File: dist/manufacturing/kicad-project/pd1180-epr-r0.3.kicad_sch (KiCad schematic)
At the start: 0 parts

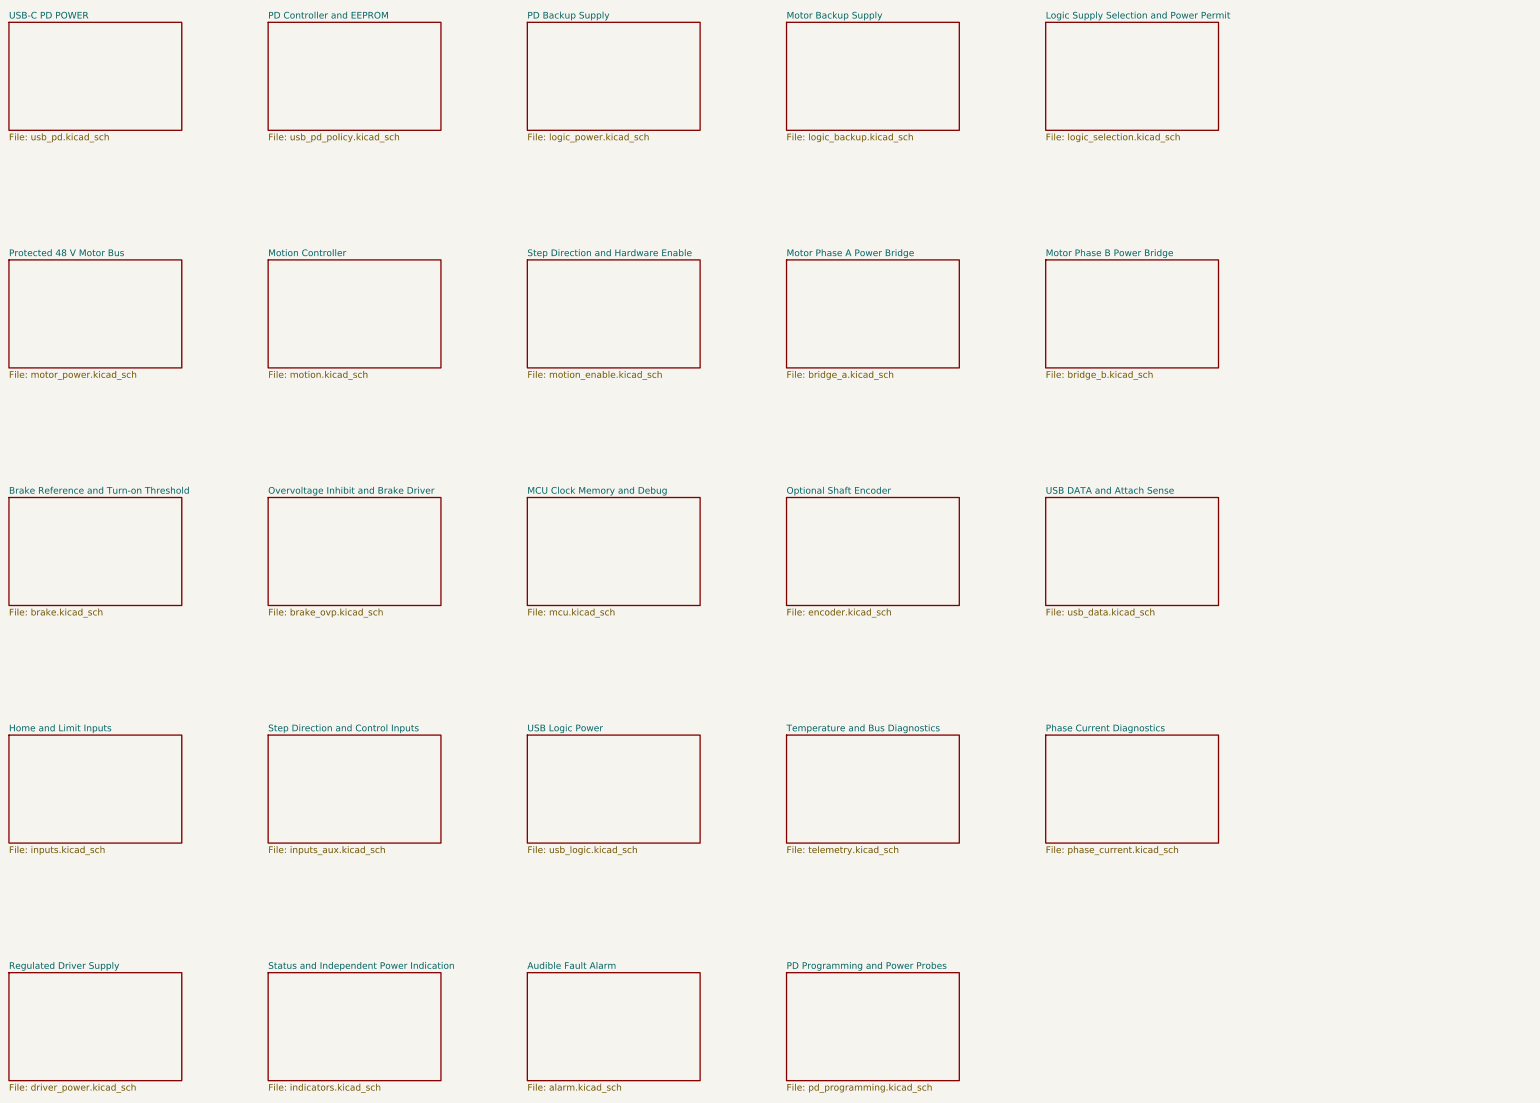
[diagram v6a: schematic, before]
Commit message: Replace J7 with onboard control and simplify motor assembly
Add local START/STOP and fail-closed motion firmware, remove unsupported external command circuitry and mounting hardware, and preserve the four PCB holes and braking protection.

Refresh native PCB routing, manufacturing files, assembly previews, and build evidence. Local source/site builds and 66 regression tests pass; sourcing, placement review, and hardware qualification remain open.
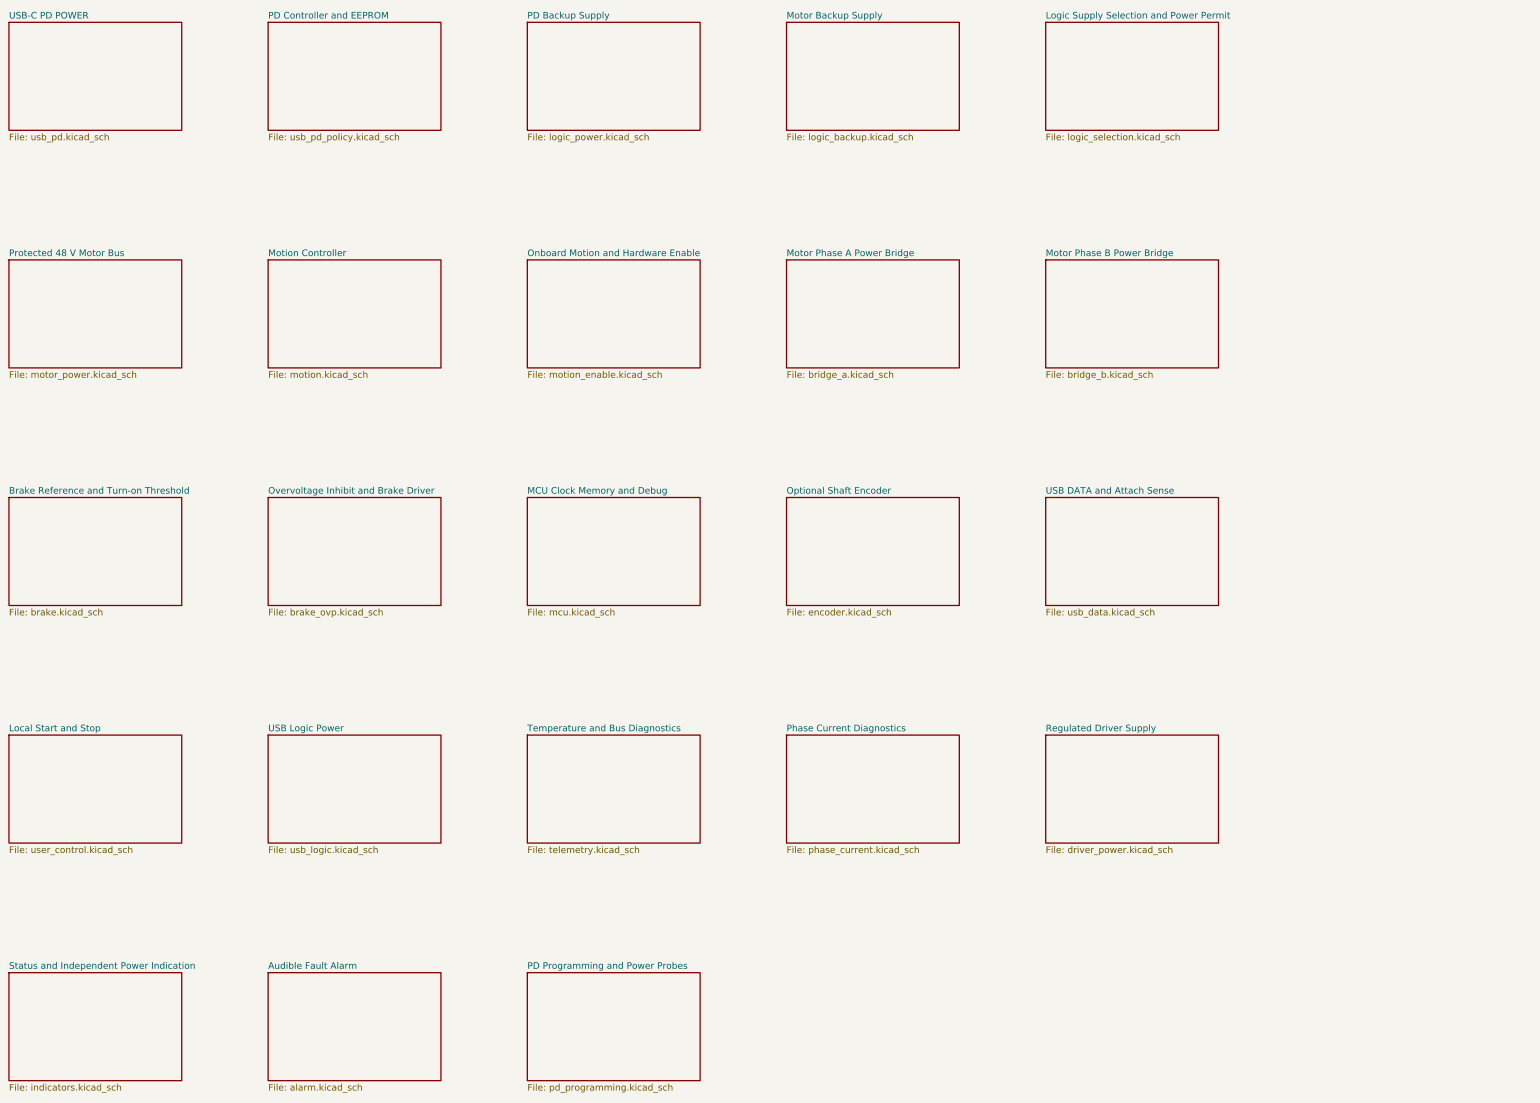
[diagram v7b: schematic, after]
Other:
- removed sheet Home and Limit Inputs
- removed sheet Step Direction and Control Inputs
- removed sheet Step Direction and Hardware Enable
- added sheet Local Start and Stop (user_control.kicad_sch)
- added sheet Onboard Motion and Hardware Enable (motion_enable.kicad_sch)
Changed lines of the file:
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@@
     (instances
       (project ""
-        (path "/32949819-0f95-4435-874f-a2b850be17d2"
+        (path "/0e244152-5dd0-4875-888f-7fba7369ce4b"
           (page "2")
         )
@@
     (instances
       (project ""
-        (path "/32949819-0f95-4435-874f-a2b850be17d2"
+        (path "/0e244152-5dd0-4875-888f-7fba7369ce4b"
           (page "3")
         )
@@
     (instances
       (project ""
-        (path "/32949819-0f95-4435-874f-a2b850be17d2"
+        (path "/0e244152-5dd0-4875-888f-7fba7369ce4b"
           (page "4")
         )
@@
     (instances
       (project ""
-        (path "/32949819-0f95-4435-874f-a2b850be17d2"
+        (path "/0e244152-5dd0-4875-888f-7fba7369ce4b"
           (page "5")
         )
@@
     (instances
       (project ""
-        (path "/32949819-0f95-4435-874f-a2b850be17d2"
+        (path "/0e244152-5dd0-4875-888f-7fba7369ce4b"
           (page "6")
         )
@@
     (instances
       (project ""
-        (path "/32949819-0f95-4435-874f-a2b850be17d2"
+        (path "/0e244152-5dd0-4875-888f-7fba7369ce4b"
           (page "7")
         )
@@
     (instances
       (project ""
-        (path "/32949819-0f95-4435-874f-a2b850be17d2"
+        (path "/0e244152-5dd0-4875-888f-7fba7369ce4b"
           (page "8")
         )
@@
       (color 0 0 0 0)
     )
-    (property "Sheetname" "Step Direction and Hardware Enable"
+    (property "Sheetname" "Onboard Motion and Hardware Enable"
       (id 0)
       (at 145.4 79.7 0)
@@
     (instances
       (project ""
-        (path "/32949819-0f95-4435-874f-a2b850be17d2"
+        (path "/0e244152-5dd0-4875-888f-7fba7369ce4b"
           (page "9")
         )
@@
     (instances
       (project ""
-        (path "/32949819-0f95-4435-874f-a2b850be17d2"
+        (path "/0e244152-5dd0-4875-888f-7fba7369ce4b"
           (page "10")
         )
@@
     (instances
       (project ""
-        (path "/32949819-0f95-4435-874f-a2b850be17d2"
+        (path "/0e244152-5dd0-4875-888f-7fba7369ce4b"
           (page "11")
         )
@@
     (instances
       (project ""
-        (path "/32949819-0f95-4435-874f-a2b850be17d2"
+        (path "/0e244152-5dd0-4875-888f-7fba7369ce4b"
           (page "12")
         )
@@
     (instances
       (project ""
-        (path "/32949819-0f95-4435-874f-a2b850be17d2"
+        (path "/0e244152-5dd0-4875-888f-7fba7369ce4b"
           (page "13")
         )
@@
     (instances
       (project ""
-        (path "/32949819-0f95-4435-874f-a2b850be17d2"
+        (path "/0e244152-5dd0-4875-888f-7fba7369ce4b"
           (page "14")
         )
@@
     (instances
       (project ""
-        (path "/32949819-0f95-4435-874f-a2b850be17d2"
+        (path "/0e244152-5dd0-4875-888f-7fba7369ce4b"
           (page "15")
         )
@@
     (instances
       (project ""
-        (path "/32949819-0f95-4435-874f-a2b850be17d2"
+        (path "/0e244152-5dd0-4875-888f-7fba7369ce4b"
           (page "16")
         )
@@
       (color 0 0 0 0)
     )
-    (property "Sheetname" "Home and Limit Inputs"
+    (property "Sheetname" "Local Start and Stop"
       (id 0)
       (at 25.4 189.70000000000002 0)
@@
       )
     )
-    (property "Sheetfile" "inputs.kicad_sch"
+    (property "Sheetfile" "user_control.kicad_sch"
       (id 1)
       (at 25.4 216.1 0)
@@
     (instances
       (project ""
-        (path "/32949819-0f95-4435-874f-a2b850be17d2"
+        (path "/0e244152-5dd0-4875-888f-7fba7369ce4b"
           (page "17")
         )
@@
       (color 0 0 0 0)
     )
-    (property "Sheetname" "Step Direction and Control Inputs"
+    (property "Sheetname" "USB Logic Power"
       (id 0)
       (at 85.4 189.70000000000002 0)
@@
       )
     )
-    (property "Sheetfile" "inputs_aux.kicad_sch"
+    (property "Sheetfile" "usb_logic.kicad_sch"
       (id 1)
       (at 85.4 216.1 0)
@@
     (instances
       (project ""
-        (path "/32949819-0f95-4435-874f-a2b850be17d2"
+        (path "/0e244152-5dd0-4875-888f-7fba7369ce4b"
           (page "18")
         )
@@
       (color 0 0 0 0)
     )
-    (property "Sheetname" "USB Logic Power"
+    (property "Sheetname" "Temperature and Bus Diagnostics"
       (id 0)
       (at 145.4 189.70000000000002 0)
@@
       )
     )
-    (property "Sheetfile" "usb_logic.kicad_sch"
+    (property "Sheetfile" "telemetry.kicad_sch"
       (id 1)
       (at 145.4 216.1 0)
@@
     (instances
       (project ""
-        (path "/32949819-0f95-4435-874f-a2b850be17d2"
+        (path "/0e244152-5dd0-4875-888f-7fba7369ce4b"
           (page "19")
         )
@@
       (color 0 0 0 0)
     )
-    (property "Sheetname" "Temperature and Bus Diagnostics"
+    (property "Sheetname" "Phase Current Diagnostics"
       (id 0)
       (at 205.4 189.70000000000002 0)
@@
       )
     )
-    (property "Sheetfile" "telemetry.kicad_sch"
+    (property "Sheetfile" "phase_current.kicad_sch"
       (id 1)
       (at 205.4 216.1 0)
@@
     (instances
       (project ""
-        (path "/32949819-0f95-4435-874f-a2b850be17d2"
+        (path "/0e244152-5dd0-4875-888f-7fba7369ce4b"
           (page "20")
         )
@@
       (color 0 0 0 0)
     )
-    (property "Sheetname" "Phase Current Diagnostics"
+    (property "Sheetname" "Regulated Driver Supply"
       (id 0)
       (at 265.4 189.70000000000002 0)
@@
       )
     )
-    (property "Sheetfile" "phase_current.kicad_sch"
+    (property "Sheetfile" "driver_power.kicad_sch"
       (id 1)
       (at 265.4 216.1 0)
@@
     (instances
       (project ""
-        (path "/32949819-0f95-4435-874f-a2b850be17d2"
+        (path "/0e244152-5dd0-4875-888f-7fba7369ce4b"
           (page "21")
         )
@@
       (color 0 0 0 0)
     )
-    (property "Sheetname" "Regulated Driver Supply"
+    (property "Sheetname" "Status and Independent Power Indication"
       (id 0)
       (at 25.4 244.70000000000002 0)
@@
       )
     )
-    (property "Sheetfile" "driver_power.kicad_sch"
+    (property "Sheetfile" "indicators.kicad_sch"
       (id 1)
       (at 25.4 271.09999999999997 0)
@@
     (instances
       (project ""
-        (path "/32949819-0f95-4435-874f-a2b850be17d2"
+        (path "/0e244152-5dd0-4875-888f-7fba7369ce4b"
           (page "22")
         )
@@
       (color 0 0 0 0)
     )
-    (property "Sheetname" "Status and Independent Power Indication"
+    (property "Sheetname" "Audible Fault Alarm"
       (id 0)
       (at 85.4 244.70000000000002 0)
@@
       )
     )
-    (property "Sheetfile" "indicators.kicad_sch"
+    (property "Sheetfile" "alarm.kicad_sch"
       (id 1)
       (at 85.4 271.09999999999997 0)
@@
     (instances
       (project ""
-        (path "/32949819-0f95-4435-874f-a2b850be17d2"
+        (path "/0e244152-5dd0-4875-888f-7fba7369ce4b"
           (page "23")
         )
@@
       (color 0 0 0 0)
     )
-    (property "Sheetname" "Audible Fault Alarm"
+    (property "Sheetname" "PD Programming and Power Probes"
       (id 0)
       (at 145.4 244.70000000000002 0)
@@
       )
     )
-    (property "Sheetfile" "alarm.kicad_sch"
+    (property "Sheetfile" "pd_programming.kicad_sch"
       (id 1)
       (at 145.4 271.09999999999997 0)
@@
     (instances
       (project ""
-        (path "/32949819-0f95-4435-874f-a2b850be17d2"
+        (path "/0e244152-5dd0-4875-888f-7fba7369ce4b"
           (page "24")
         )
       )
-    )
-  )
-  (sheet
-    (at 205.4 245.4)
-    (size 40 25)
-    (exclude_from_sim no)
-    (in_bom yes)
-    (on_board yes)
-    (dnp no)
-    (fields_autoplaced yes)
-    (stroke
-      (width 0.1524)
-      (type solid)
-    )
-    (fill
-      (color 0 0 0 0)
-    )
-    (property "Sheetname" "PD Programming and Power Probes"
-      (id 0)
-      (at 205.4 244.70000000000002 0)
-      (effects
-        (font
-          (size 1.524 1.524)
-        )
-        (justify left bottom)
-      )
-    )
-    (property "Sheetfile" "pd_programming.kicad_sch"
-      (id 1)
-      (at 205.4 271.09999999999997 0)
-      (effects
-        (font
-          (size 1.524 1.524)
-        )
-        (justify left top)
-      )
-    )
-    (instances
-      (project ""
-        (path "/32949819-0f95-4435-874f-a2b850be17d2"
-          (page "25")
-        )
-      )

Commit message: Add power and brake protection ECO for the ordered NEMA34 motor
Use TPS26630 1x latch-off current limiting at 4.27 A nominal and lower the
motor inhibit threshold to 53.18 V. Add a 100 V brake-cable clamp and ADC
startup continuity feedback, with a 3.8 A RMS motor-current ceiling and
locked 0.827 A / 10 rpm unloaded commissioning profile.

Update the native PCB, 24-sheet schematic, firmware, calculations, nine
behavioral simulation cases and engineering delivery artifacts. Preserve
unrelated component geometry and all four mounting holes.

Native DRC/ERC/parity, connectivity, critical copper, power routing,
firmware tests and STM32 image checks pass. Full verification retains
three failing groups: existing C23/R56/C41 placement advisories and
assembly/standards sourcing evidence. Ordering and powered qualification
remain held; brake continuity is a startup check, not runtime protection.
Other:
- added sheet Brake Continuity Preflight (brake_feedback.kicad_sch)
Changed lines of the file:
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@@
     (instances
       (project ""
-        (path "/0e244152-5dd0-4875-888f-7fba7369ce4b"
+        (path "/495e3eb3-9d45-44b1-ad31-ea992674a5e1"
           (page "2")
         )
@@
     (instances
       (project ""
-        (path "/0e244152-5dd0-4875-888f-7fba7369ce4b"
+        (path "/495e3eb3-9d45-44b1-ad31-ea992674a5e1"
           (page "3")
         )
@@
     (instances
       (project ""
-        (path "/0e244152-5dd0-4875-888f-7fba7369ce4b"
+        (path "/495e3eb3-9d45-44b1-ad31-ea992674a5e1"
           (page "4")
         )
@@
     (instances
       (project ""
-        (path "/0e244152-5dd0-4875-888f-7fba7369ce4b"
+        (path "/495e3eb3-9d45-44b1-ad31-ea992674a5e1"
           (page "5")
         )
@@
     (instances
       (project ""
-        (path "/0e244152-5dd0-4875-888f-7fba7369ce4b"
+        (path "/495e3eb3-9d45-44b1-ad31-ea992674a5e1"
           (page "6")
         )
@@
     (instances
       (project ""
-        (path "/0e244152-5dd0-4875-888f-7fba7369ce4b"
+        (path "/495e3eb3-9d45-44b1-ad31-ea992674a5e1"
           (page "7")
         )
@@
     (instances
       (project ""
-        (path "/0e244152-5dd0-4875-888f-7fba7369ce4b"
+        (path "/495e3eb3-9d45-44b1-ad31-ea992674a5e1"
           (page "8")
         )
@@
     (instances
       (project ""
-        (path "/0e244152-5dd0-4875-888f-7fba7369ce4b"
+        (path "/495e3eb3-9d45-44b1-ad31-ea992674a5e1"
           (page "9")
         )
@@
     (instances
       (project ""
-        (path "/0e244152-5dd0-4875-888f-7fba7369ce4b"
+        (path "/495e3eb3-9d45-44b1-ad31-ea992674a5e1"
           (page "10")
         )
@@
     (instances
       (project ""
-        (path "/0e244152-5dd0-4875-888f-7fba7369ce4b"
+        (path "/495e3eb3-9d45-44b1-ad31-ea992674a5e1"
           (page "11")
         )
@@
     (instances
       (project ""
-        (path "/0e244152-5dd0-4875-888f-7fba7369ce4b"
+        (path "/495e3eb3-9d45-44b1-ad31-ea992674a5e1"
           (page "12")
         )
@@
     (instances
       (project ""
-        (path "/0e244152-5dd0-4875-888f-7fba7369ce4b"
+        (path "/495e3eb3-9d45-44b1-ad31-ea992674a5e1"
           (page "13")
         )
@@
     (instances
       (project ""
-        (path "/0e244152-5dd0-4875-888f-7fba7369ce4b"
+        (path "/495e3eb3-9d45-44b1-ad31-ea992674a5e1"
           (page "14")
         )
@@
     (instances
       (project ""
-        (path "/0e244152-5dd0-4875-888f-7fba7369ce4b"
+        (path "/495e3eb3-9d45-44b1-ad31-ea992674a5e1"
           (page "15")
         )
@@
     (instances
       (project ""
-        (path "/0e244152-5dd0-4875-888f-7fba7369ce4b"
+        (path "/495e3eb3-9d45-44b1-ad31-ea992674a5e1"
           (page "16")
         )
@@
     (instances
       (project ""
-        (path "/0e244152-5dd0-4875-888f-7fba7369ce4b"
+        (path "/495e3eb3-9d45-44b1-ad31-ea992674a5e1"
           (page "17")
         )
@@
     (instances
       (project ""
-        (path "/0e244152-5dd0-4875-888f-7fba7369ce4b"
+        (path "/495e3eb3-9d45-44b1-ad31-ea992674a5e1"
           (page "18")
         )
@@
     (instances
       (project ""
-        (path "/0e244152-5dd0-4875-888f-7fba7369ce4b"
+        (path "/495e3eb3-9d45-44b1-ad31-ea992674a5e1"
           (page "19")
         )
@@
     (instances
       (project ""
-        (path "/0e244152-5dd0-4875-888f-7fba7369ce4b"
+        (path "/495e3eb3-9d45-44b1-ad31-ea992674a5e1"
           (page "20")
         )
@@
     (instances
       (project ""
-        (path "/0e244152-5dd0-4875-888f-7fba7369ce4b"
+        (path "/495e3eb3-9d45-44b1-ad31-ea992674a5e1"
           (page "21")
         )
@@
     (instances
       (project ""
-        (path "/0e244152-5dd0-4875-888f-7fba7369ce4b"
+        (path "/495e3eb3-9d45-44b1-ad31-ea992674a5e1"
           (page "22")
         )
@@
     (instances
       (project ""
-        (path "/0e244152-5dd0-4875-888f-7fba7369ce4b"
+        (path "/495e3eb3-9d45-44b1-ad31-ea992674a5e1"
           (page "23")
         )
@@
     (instances
       (project ""
-        (path "/0e244152-5dd0-4875-888f-7fba7369ce4b"
+        (path "/495e3eb3-9d45-44b1-ad31-ea992674a5e1"
           (page "24")
         )
       )
+    )
+  )
+  (sheet
+    (at 205.4 245.4)
+    (size 40 25)
+    (exclude_from_sim no)
+    (in_bom yes)
+    (on_board yes)
+    (dnp no)
+    (fields_autoplaced yes)
+    (stroke
+      (width 0.1524)
+      (type solid)
+    )
+    (fill
+      (color 0 0 0 0)
+    )
+    (property "Sheetname" "Brake Continuity Preflight"
+      (id 0)
+      (at 205.4 244.70000000000002 0)
+      (effects
+        (font
+          (size 1.524 1.524)
+        )
+        (justify left bottom)
+      )
+    )
+    (property "Sheetfile" "brake_feedback.kicad_sch"
+      (id 1)
+      (at 205.4 271.09999999999997 0)
+      (effects
+        (font
+          (size 1.524 1.524)
+        )
+        (justify left top)
+      )
+    )
+    (instances
+      (project ""
+        (path "/495e3eb3-9d45-44b1-ad31-ea992674a5e1"
+          (page "25")
+        )
+      )
